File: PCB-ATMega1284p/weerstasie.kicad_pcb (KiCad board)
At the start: 2 copper layers, 40 parts, among them J1 WIND, J10 Conn_01x01, J11 Conn_01x01, J12 Conn_01x01, J13 Conn_01x01, J2 batt -, J3 batt +, J4 RAIN, J5 Conn_01x01, J6 Conn_01x01, J7 INT2, J8 I2C, J9 UART, SW1 SW_Push, U1 BME280, U2 RFM95, U3 ATMEGA1284P-AU, Y1 8MHz

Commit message: Some PCB cleanup
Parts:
- moved C11 4.09 mm to (122.5, 96.3)
- moved J7 1.10 mm to (127.4, 79.4)
- moved J8 1.03 mm to (125.0, 102.0)
- moved J10 0.30 mm to (109.4, 86.6)
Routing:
- net GND: track 260.5 -> 364.6 mm, vias 90 -> 132
- net /MISO: track 61.2 -> 67.1 mm, vias 4 -> 3
- net VCC: track 155.2 -> 160.6 mm
- net /WIND_SPEED: track 23.0 -> 20.4 mm
- net Net-(C9-Pad1): track 3.60 -> 1.02 mm
- net /RFM_D0: track 40.6 -> 38.1 mm
- net /RESET: track 24.8 -> 26.4 mm
- net /MOSI: track 58.5 -> 57.1 mm
- net /RFM_D1: track 39.8 -> 38.5 mm
- net /SCK: track 63.9 -> 62.7 mm
- net Net-(J7-Pad1): track 10.3 -> 11.3 mm
- net /WIND_DIR: track 48.8 -> 47.9 mm
- net Net-(J8-Pad2): track 3.08 -> 2.36 mm
- net /SOLAR_1: track 26.0 -> 25.3 mm
- net /BME_SS: track 10.1 -> 10.7 mm
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
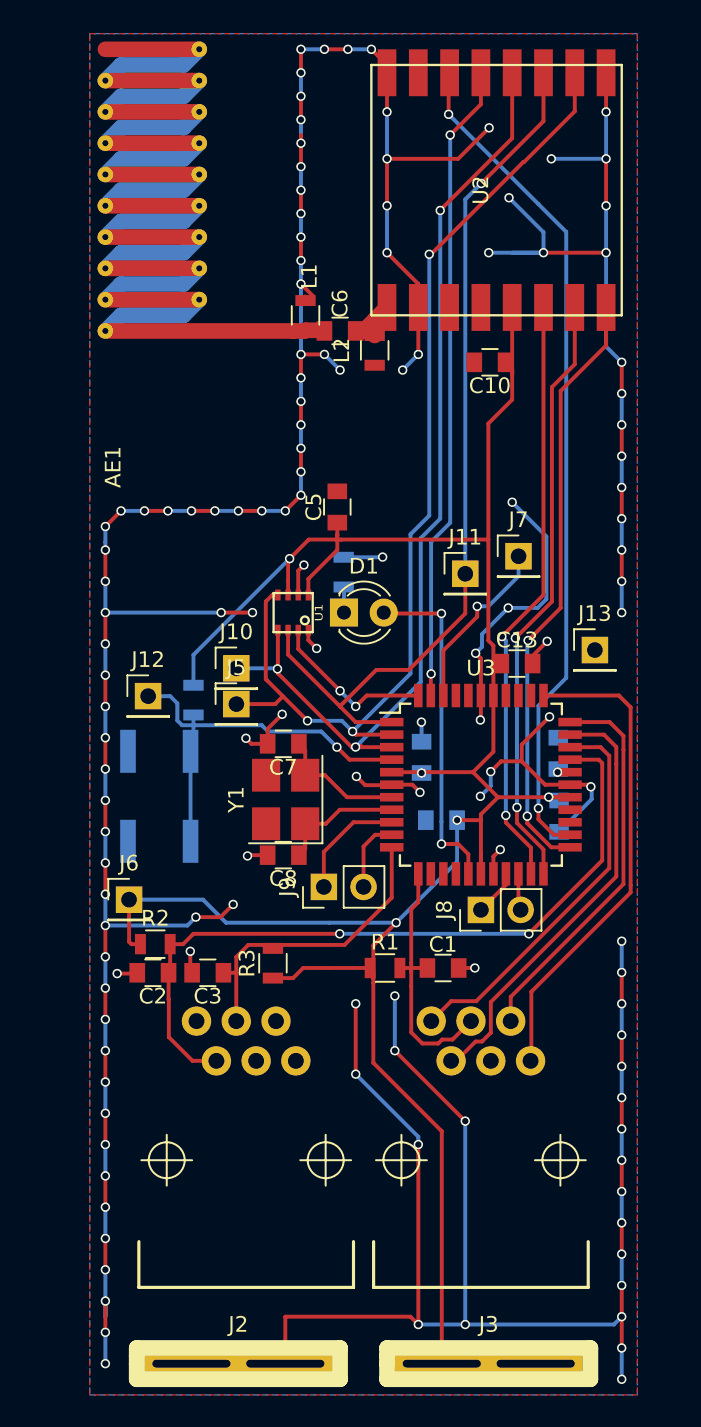
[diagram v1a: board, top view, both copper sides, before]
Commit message: More cleanup and comaptibility with allpcb
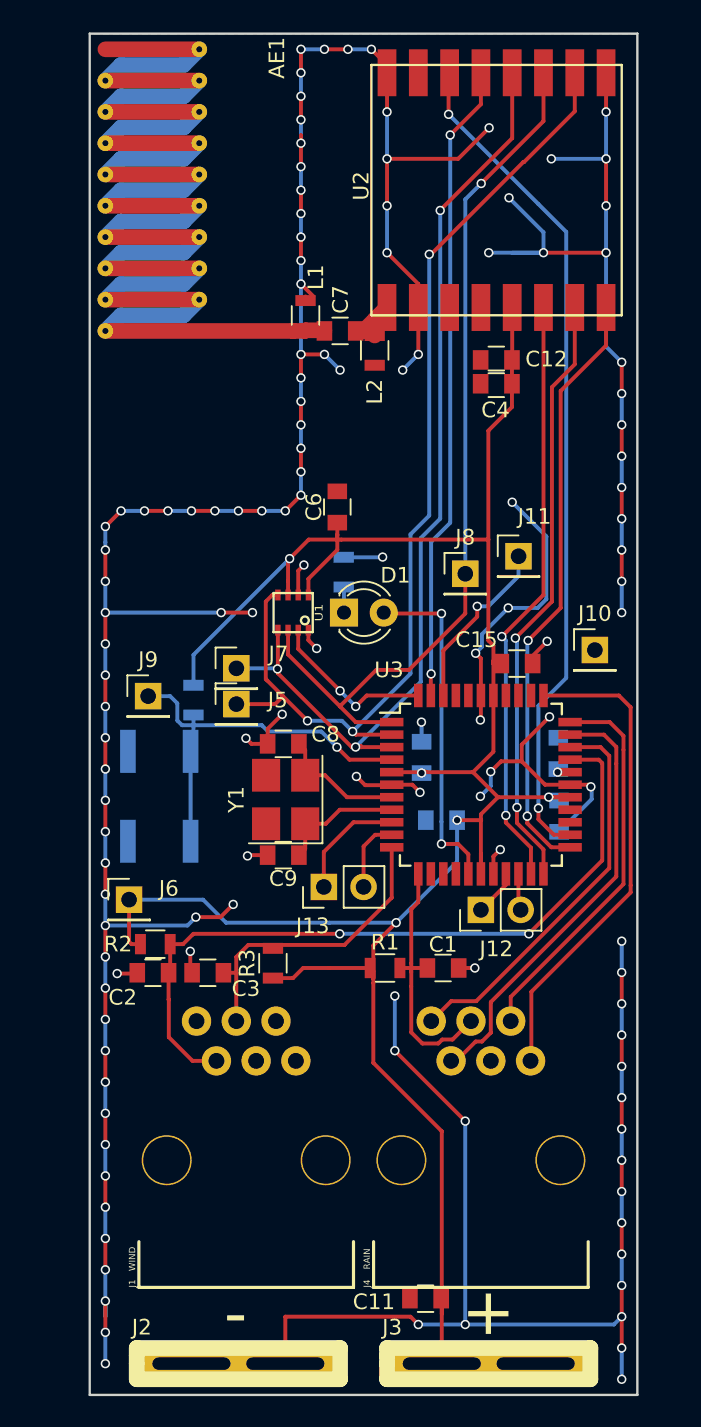
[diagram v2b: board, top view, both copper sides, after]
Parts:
- added C11: 10uF, Capacitors_SMD:C_0805, F.Cu at (121.5, 126.8)
- added C4: 10uF, Capacitors_SMD:C_0805, F.Cu at (126.0, 68.4)
- moved C12 0.43 mm to (126.0, 66.9)
- renumbered C9 to C10, C10 to C12, C11 to C13, C12 to C14, C13 to C15, C4 to C5, C5 to C6, C6 to C7, C7 to C8, C8 to C9, J13 to J10, J7 to J11, J8 to J12, J9 to J13, J10 to J7, J11 to J8, J12 to J9
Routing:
- net GND: track 364.6 -> 342.5 mm, vias 132 -> 129
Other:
- board outline added: 35 x 87 mm
- board text added: "+"
- board text added: "-"

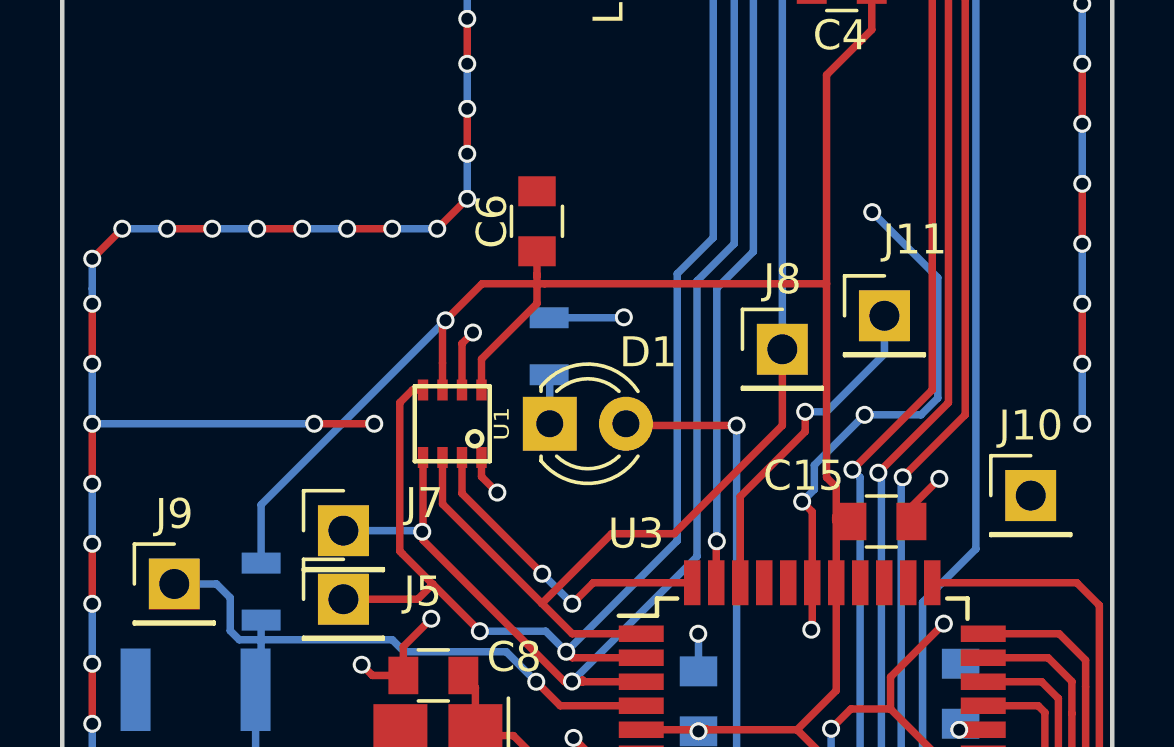
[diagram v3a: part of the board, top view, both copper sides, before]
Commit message: Add ventilation holes/vias around thermometer and resend gerbers to AllPCB
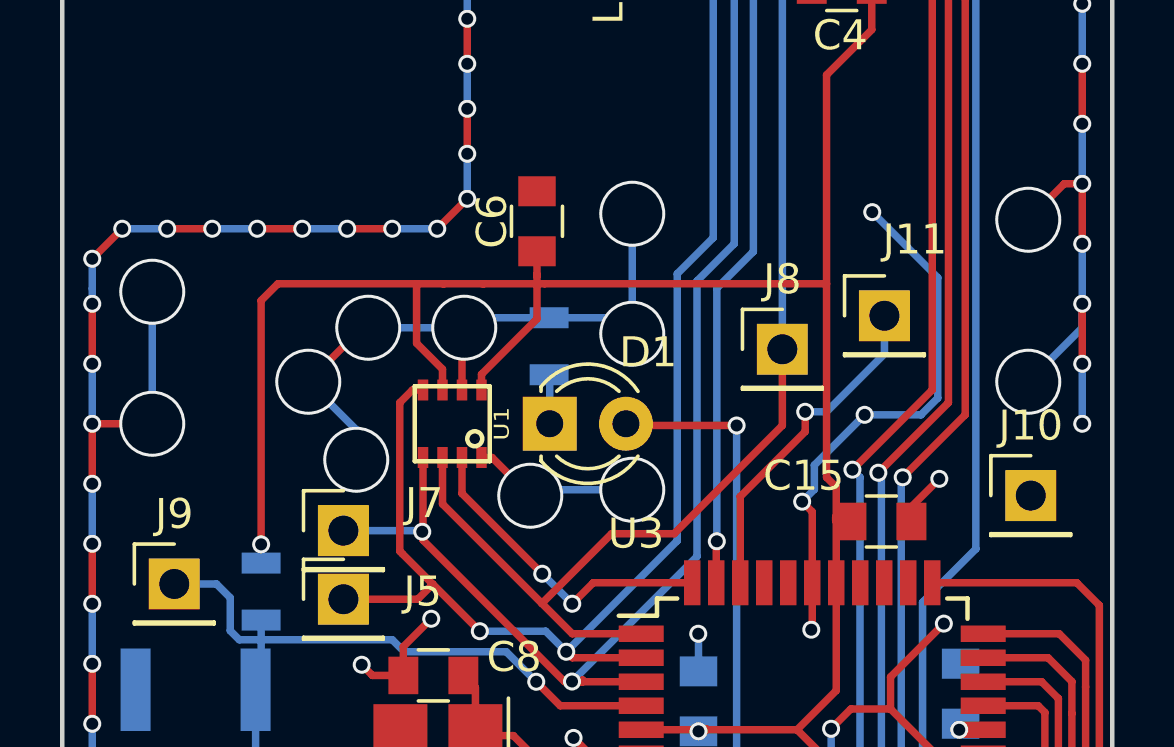
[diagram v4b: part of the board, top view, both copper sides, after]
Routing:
- net GND: track 342.5 -> 366.9 mm, vias 129 -> 136
- net VCC: track 160.6 -> 166.3 mm
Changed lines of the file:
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@@
     (links 106)
     (no_connects 0)
-    (area 75.050001 36.5 135.100001 133.100001)
+    (area 99.924999 45.924999 135.075001 133.075001)
     (thickness 1.6)
     (drawings 19)
-    (tracks 661)
+    (tracks 688)
     (zones 0)
     (modules 42)
@@
     (via_min_size 0.4)
     (via_min_drill 0.3)
+    (user_via 2.2 2)
     (uvia_size 0.3)
     (uvia_drill 0.1)
@@
   (gr_line (start 128 79) (end 107 79) (angle 90) (layer Dwgs.User) (width 0.2))
   (gr_line (start 128 91) (end 128 95) (angle 90) (layer Dwgs.User) (width 0.2))
+  (segment (start 110.2 79.8) (end 110 79.8) (width 0.25) (layer F.Cu) (net 1))
+  (via (at 109.8 84.2) (size 2.2) (drill 2) (layers F.Cu B.Cu) (net 1))
+  (segment (start 109.8 83.2) (end 109.8 84.2) (width 0.25) (layer B.Cu) (net 1))
+  (segment (start 108.2 81.6) (end 109.8 83.2) (width 0.25) (layer B.Cu) (net 1))
+  (via (at 108.2 81.6) (size 2.2) (drill 2) (layers F.Cu B.Cu) (net 1))
+  (segment (start 110 79.8) (end 108.2 81.6) (width 0.25) (layer F.Cu) (net 1))
+  (segment (start 113.975 84.125) (end 114.325 84.125) (width 0.25) (layer F.Cu) (net 1))
+  (via (at 119 85.2) (size 2.2) (drill 2) (layers F.Cu B.Cu) (net 1))
+  (segment (start 115.8 85.2) (end 119 85.2) (width 0.25) (layer B.Cu) (net 1))
+  (segment (start 115.6 85.4) (end 115.8 85.2) (width 0.25) (layer B.Cu) (net 1))
+  (via (at 115.6 85.4) (size 2.2) (drill 2) (layers F.Cu B.Cu) (net 1))
+  (segment (start 114.325 84.125) (end 115.6 85.4) (width 0.25) (layer F.Cu) (net 1))
+  (segment (start 113.325 81.875) (end 113.325 79.875) (width 0.25) (layer F.Cu) (net 1))
+  (via (at 113.4 79.8) (size 2.2) (drill 2) (layers F.Cu B.Cu) (net 1))
+  (segment (start 113.325 79.875) (end 113.4 79.8) (width 0.25) (layer F.Cu) (net 1))
+  (segment (start 134 75) (end 133.4 75) (width 0.25) (layer F.Cu) (net 1))
+  (via (at 132.2 76.2) (size 2.2) (drill 2) (layers F.Cu B.Cu) (net 1))
+  (segment (start 133.4 75) (end 132.2 76.2) (width 0.25) (layer F.Cu) (net 1))
+  (segment (start 101 83) (end 103 83) (width 0.25) (layer F.Cu) (net 1))
+  (via (at 103 78.6) (size 2.2) (drill 2) (layers F.Cu B.Cu) (net 1))
+  (segment (start 103 83) (end 103 78.6) (width 0.25) (layer B.Cu) (net 1))
+  (via (at 103 83) (size 2.2) (drill 2) (layers F.Cu B.Cu) (net 1))
+  (segment (start 134 79) (end 134 79.8) (width 0.25) (layer B.Cu) (net 1))
+  (via (at 132.2 81.6) (size 2.2) (drill 2) (layers F.Cu B.Cu) (net 1))
+  (segment (start 134 79.8) (end 132.2 81.6) (width 0.25) (layer B.Cu) (net 1))
+  (segment (start 113.4 79.8) (end 110.2 79.8) (width 0.25) (layer B.Cu) (net 1))
+  (segment (start 113.7336 79.4664) (end 113.4 79.8) (width 0.25) (layer B.Cu) (net 1))
+  (segment (start 116.2304 79.4664) (end 113.7336 79.4664) (width 0.25) (layer B.Cu) (net 1))
+  (segment (start 110.2 79.8) (end 109.6 80.4) (width 0.25) (layer F.Cu) (net 1))
+  (via (at 110.2 79.8) (size 2.2) (drill 2) (layers F.Cu B.Cu) (net 1))
+  (segment (start 119 76) (end 119 80) (width 0.25) (layer B.Cu) (net 1))
+  (segment (start 118.4664 79.4664) (end 116.2304 79.4664) (width 0.25) (layer B.Cu) (net 1))
+  (segment (start 119 80) (end 118.4664 79.4664) (width 0.25) (layer B.Cu) (net 1))
+  (via (at 119 80) (size 2.2) (drill 2) (layers F.Cu B.Cu) (net 1))
+  (via (at 119 76) (size 2.2) (drill 2) (layers F.Cu B.Cu) (net 1))
   (segment (start 129 60) (end 129 58.6928) (width 0.25) (layer B.Cu) (net 1))
   (via (at 126.7968 56.4896) (size 0.6) (drill 0.4) (layers F.Cu B.Cu) (net 1))
@@
   (via (at 126.746 82.7024) (size 0.6) (drill 0.4) (layers F.Cu B.Cu) (net 1))
   (segment (start 126.746 82.7024) (end 126.746 82.6516) (width 0.25) (layer F.Cu) (net 1))
-  (segment (start 116.2304 79.4664) (end 118.7044 79.4664) (width 0.25) (layer B.Cu) (net 1))
-  (via (at 118.7196 79.4512) (size 0.6) (drill 0.4) (layers F.Cu B.Cu) (net 1))
-  (segment (start 118.7044 79.4664) (end 118.7196 79.4512) (width 0.25) (layer B.Cu) (net 1))
-  (segment (start 113.325 81.875) (end 113.325 80.3246) (width 0.25) (layer F.Cu) (net 1))
-  (via (at 113.6904 79.9592) (size 0.6) (drill 0.4) (layers F.Cu B.Cu) (net 1))
-  (segment (start 113.325 80.3246) (end 113.6904 79.9592) (width 0.25) (layer F.Cu) (net 1))
-  (segment (start 101 83) (end 108.4 83) (width 0.25) (layer B.Cu) (net 1))
-  (via (at 110.4 83) (size 0.6) (drill 0.4) (layers F.Cu B.Cu) (net 1))
-  (segment (start 108.4 83) (end 110.4 83) (width 0.25) (layer F.Cu) (net 1))
-  (via (at 108.4 83) (size 0.6) (drill 0.4) (layers F.Cu B.Cu) (net 1))
   (segment (start 134 104) (end 134 106) (width 0.25) (layer B.Cu) (net 1))
   (via (at 134 126) (size 0.6) (drill 0.4) (layers F.Cu B.Cu) (net 1))
@@
   (segment (start 114.292 62.792) (end 113.5 62) (width 0.25) (layer F.Cu) (net 1))
   (via (at 113.5 62) (size 0.6) (drill 0.4) (layers F.Cu B.Cu) (net 1))
-  (segment (start 113.975 84.125) (end 113.975 84.765) (width 0.25) (layer F.Cu) (net 1))
-  (via (at 114.5032 85.2932) (size 0.6) (drill 0.4) (layers F.Cu B.Cu) (net 1))
-  (segment (start 113.975 84.765) (end 114.5032 85.2932) (width 0.25) (layer F.Cu) (net 1))
   (segment (start 111.3696 91.3892) (end 110.3376 91.3892) (width 0.25) (layer F.Cu) (net 1))
   (via (at 109.982 91.0336) (size 0.6) (drill 0.4) (layers F.Cu B.Cu) (net 1))
@@
   (segment (start 113 65) (end 113.75 65) (width 1) (layer F.Cu) (net 2))
   (segment (start 113.75 65) (end 113.792 64.958) (width 1) (layer F.Cu) (net 2))
+  (segment (start 112.675 81.875) (end 112.675 81.179) (width 0.25) (layer F.Cu) (net 3))
+  (segment (start 111.8108 80.3148) (end 111.8108 78.3336) (width 0.25) (layer F.Cu) (net 3))
+  (segment (start 112.675 81.179) (end 111.8108 80.3148) (width 0.25) (layer F.Cu) (net 3))
+  (segment (start 112.675 78.3336) (end 112.7252 78.3336) (width 0.25) (layer F.Cu) (net 3))
+  (segment (start 114.046 78.3336) (end 112.7252 78.3336) (width 0.25) (layer F.Cu) (net 3))
+  (segment (start 112.7252 78.3336) (end 111.8108 78.3336) (width 0.25) (layer F.Cu) (net 3))
+  (segment (start 111.8108 78.3336) (end 107.188 78.3336) (width 0.25) (layer F.Cu) (net 3))
+  (segment (start 106.6292 87.0204) (end 106.6292 87.6452) (width 0.25) (layer B.Cu) (net 3))
+  (via (at 106.6292 87.0204) (size 0.6) (drill 0.4) (layers F.Cu B.Cu) (net 3))
+  (segment (start 106.6292 78.8924) (end 106.6292 87.0204) (width 0.25) (layer F.Cu) (net 3))
+  (segment (start 107.188 78.3336) (end 106.6292 78.8924) (width 0.25) (layer F.Cu) (net 3))
   (segment (start 122.5 127.8128) (end 122.5 126.8848) (width 0.25) (layer F.Cu) (net 3))
   (segment (start 122.5 126.8848) (end 122.4628 126.8476) (width 0.25) (layer F.Cu) (net 3))
@@
   (segment (start 125 96.266) (end 125.0188 96.266) (width 0.25) (layer F.Cu) (net 3))
   (segment (start 125.0188 96.266) (end 125 96.266) (width 0.25) (layer F.Cu) (net 3))
-  (segment (start 113.975 81.875) (end 113.975 80.843) (width 0.25) (layer F.Cu) (net 3))
-  (segment (start 115.824 78.994) (end 115.824 78.3336) (width 0.25) (layer F.Cu) (net 3))
-  (segment (start 113.975 80.843) (end 115.824 78.994) (width 0.25) (layer F.Cu) (net 3))
+  (segment (start 113.975 81.875) (end 113.975 81.351) (width 0.25) (layer F.Cu) (net 3))
+  (segment (start 115.824 79.502) (end 115.824 78.3336) (width 0.25) (layer F.Cu) (net 3))
+  (segment (start 113.975 81.351) (end 115.824 79.502) (width 0.25) (layer F.Cu) (net 3))
   (segment (start 103.2408 104.1908) (end 102.6668 104.1908) (width 0.25) (layer F.Cu) (net 3))
   (segment (start 102.5144 104.0384) (end 102.5144 101.346) (width 0.25) (layer F.Cu) (net 3))
@@
   (segment (start 115.824 77.2508) (end 115.824 78.0288) (width 0.25) (layer F.Cu) (net 3))
   (segment (start 115.824 78.0288) (end 115.824 78.0796) (width 0.25) (layer F.Cu) (net 3))
-  (via (at 112.776 79.5528) (size 0.6) (drill 0.4) (layers F.Cu B.Cu) (net 3))
-  (segment (start 106.6292 87.6452) (end 106.6292 85.6996) (width 0.25) (layer B.Cu) (net 3))
-  (segment (start 106.6292 85.6996) (end 112.776 79.5528) (width 0.25) (layer B.Cu) (net 3))
-  (segment (start 112.675 81.875) (end 112.675 80.9752) (width 0.25) (layer F.Cu) (net 3))
-  (segment (start 112.675 80.9752) (end 112.675 79.6538) (width 0.25) (layer F.Cu) (net 3))
-  (segment (start 113.9952 78.3336) (end 115.824 78.3336) (width 0.25) (layer F.Cu) (net 3))
-  (segment (start 112.776 79.5528) (end 113.9952 78.3336) (width 0.25) (layer F.Cu) (net 3))
+  (segment (start 113.9952 78.3336) (end 114.046 78.3336) (width 0.25) (layer F.Cu) (net 3))
+  (segment (start 114.046 78.3336) (end 115.824 78.3336) (width 0.25) (layer F.Cu) (net 3))
   (segment (start 115.824 78.3336) (end 116.078 78.3336) (width 0.25) (layer F.Cu) (net 3))
   (segment (start 116.078 78.3336) (end 125.476 78.3336) (width 0.25) (layer F.Cu) (net 3))
-  (segment (start 112.675 79.6538) (end 112.776 79.5528) (width 0.25) (layer F.Cu) (net 3))
   (segment (start 125.8 88.3) (end 125.8 86.106) (width 0.25) (layer F.Cu) (net 3))
   (segment (start 125.8 86.106) (end 125.8 85.1092) (width 0.25) (layer F.Cu) (net 3))
